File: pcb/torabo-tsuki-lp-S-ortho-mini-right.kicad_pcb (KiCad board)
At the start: 2 copper layers, 138.8 x 74 mm, 67 parts, among them J201 Conn_01x06_MountingPin, SW201 SW_SPDT, SW43 SW_Push, SW44 SW_Push, SW45 SW_Push, SW46 SW_Push, SW47 SW_Push, SW48 SW_Push, SW50 SW_Push, SW51 SW_Push, SW52 SW_Push, SW53 SW_Push, SW54 SW_Push, SW55 SW_Push, SW57 SW_Push, SW58 SW_Push, SW59 SW_Push, SW60 SW_Push, SW61 SW_Push, SW62 SW_Push, SW63 SW_Push, SW64 SW_Push, SW65 SW_Push, SW69 SW_Push, SW70 SW_Push, U201 XIAO nRF52840 Plus, U202 AE-XCL103-5V0, U203 XC8111AA01MR-G

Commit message: Rename PCB silkscreen to kb-1
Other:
- board text added: "kb-1"
- board text removed: "torabo-tsuki om(s) v0"
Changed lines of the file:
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@@
 		)
 	)
-	(gr_text "torabo-tsuki om(s) v0"
+	(gr_text "kb-1"
 		(at 43.1 150.9 0)
 		(layer "F.SilkS")

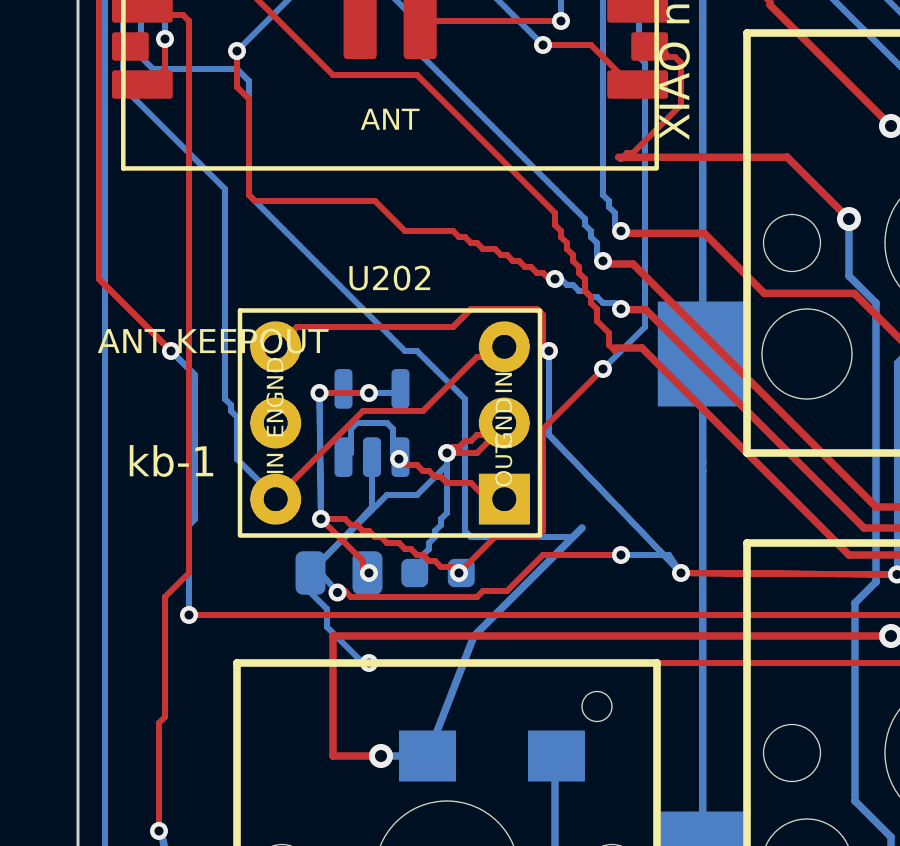
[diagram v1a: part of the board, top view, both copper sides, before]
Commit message: Add right-side boost circuit to PCBA
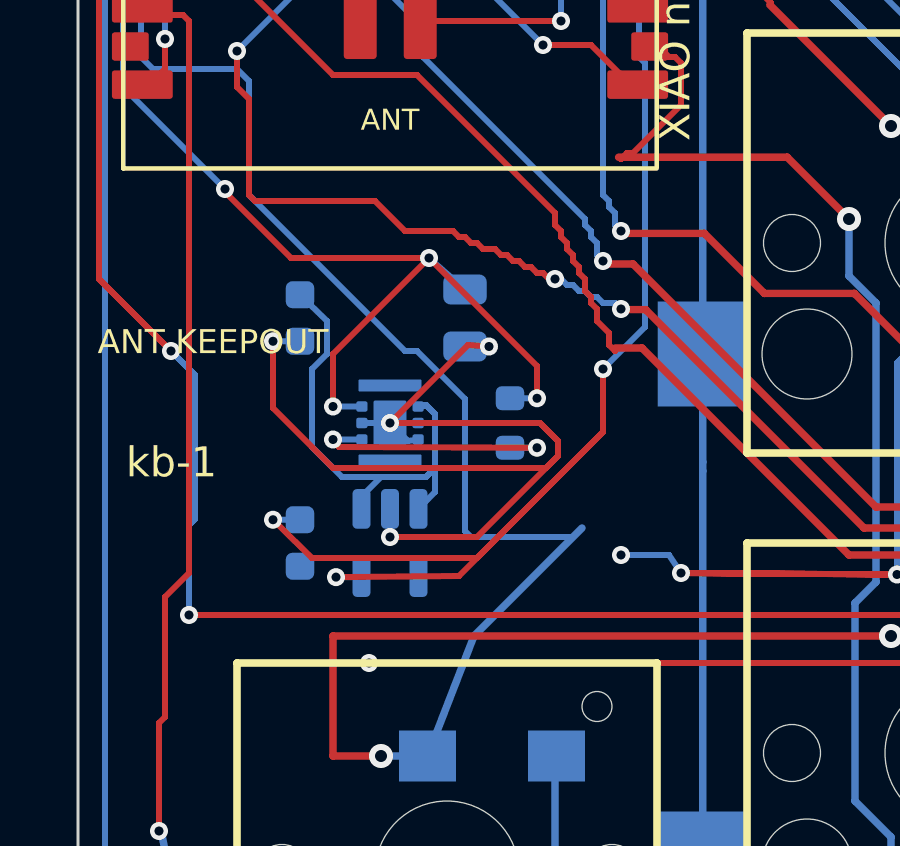
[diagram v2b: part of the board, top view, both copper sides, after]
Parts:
- added C204: 0.1uF 50V X7R, C_0603_1608Metric, B.Cu at (48.9, 153.0)
- added R202: 100k, R_0603_1608Metric, B.Cu at (55.9, 149.0)
- C202: value 0.1uF 50V X7R -> 10uF 16V X5R
- U202: value AE-XCL103-5V0 -> XCL103D503CR-G; footprint Library:AE-XCL103-5V0 -> CL-2025-02; moved to B.Cu
- moved C202 9.66 mm to (48.9, 145.5), turned to -90 degrees
- moved C201 9.48 mm to (54.4, 145.5), turned to -90 degrees
- moved U203 4.04 mm to (51.9, 153.0), turned to -90 degrees
- turned U202 to -90 degrees
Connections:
- C201 pad 1: /right/SYS_5V -> +BATT
- C202 pad 1: /right/SYS_5V -> /right/BOOST_5V
- U202 pad 1: GND -> +BATT
- U202 pad 2: (no net) -> GND
- U202 pad 3: +BATT -> /right/BOOST_EN
- U202 pad 4: +BATT -> GND
- U202 pad 5: GND -> (no net)
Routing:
- net GND: track 393.3 -> 358.5 mm, vias 17 -> 18
- net /right/BOOST_5V: track 8.26 -> 22.6 mm, vias 1 -> 0
- net /right/BOOST_EN: track 0.00 -> 8.78 mm, vias 0 -> 2
- net +BATT: track 50.5 -> 52.9 mm, vias 2 -> 6
- net /right/SYS_5V: track 57.5 -> 56.0 mm, vias 7 -> 4

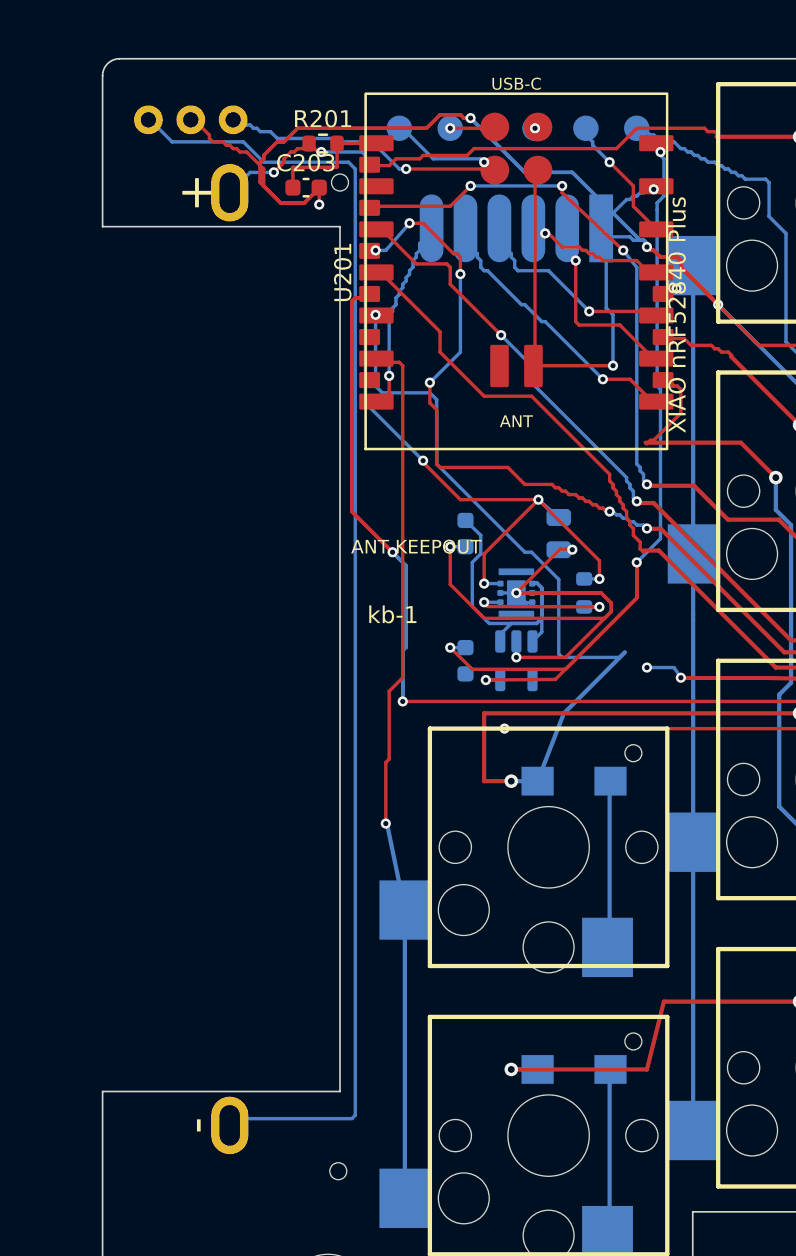
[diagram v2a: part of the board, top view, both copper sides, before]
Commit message: WIP: checkpoint single-XIAO PCB and vertical PHD conversion
Preserve the current single-controller PCB, schematics, documentation, and manufacturing artifacts. Include the vertical PHD placement/routing experiment; its candidate boards still fail DRC and are not production-ready.
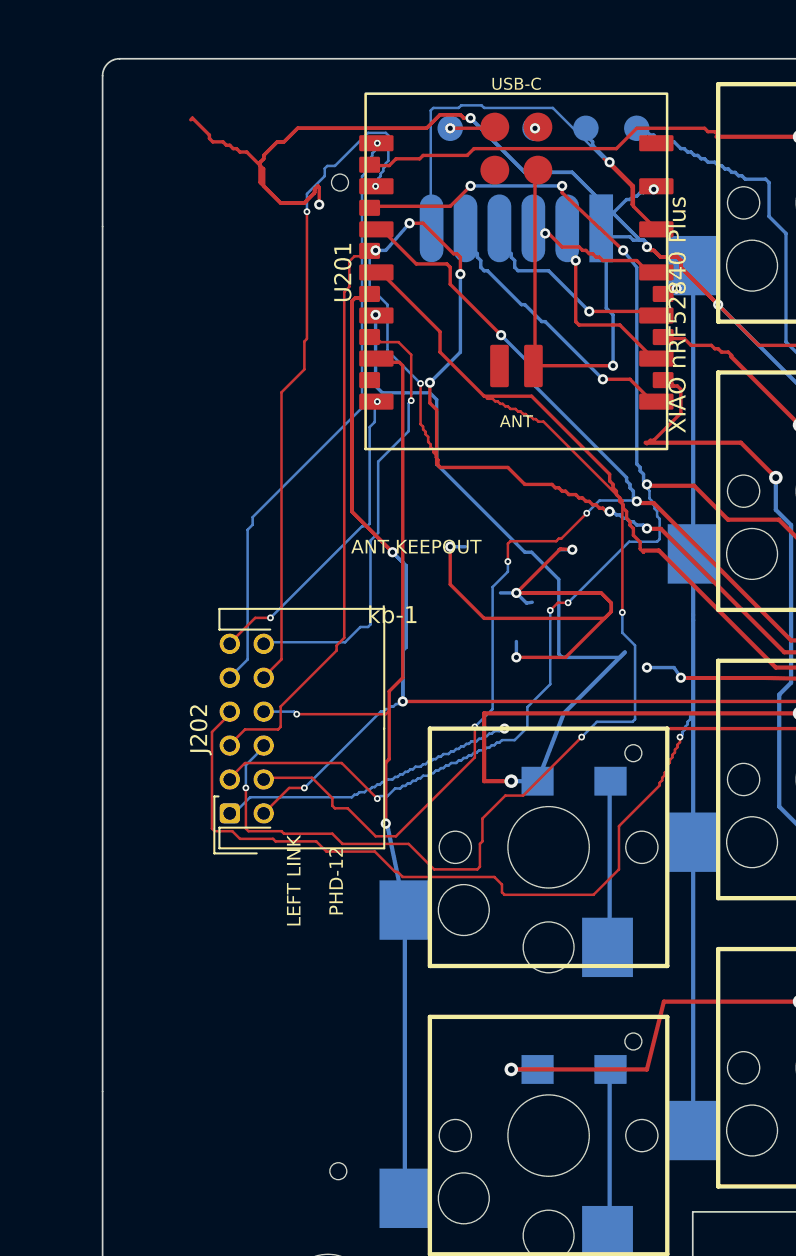
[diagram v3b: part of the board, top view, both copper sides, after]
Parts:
- removed BT201: GB-BH-4X1-WP, Library:battery_holder_AAA_1x_P55mm
- removed C201: 10uF 25V X5R, C_0805_2012Metric
- removed C202: 10uF 16V X5R, C_0603_1608Metric
- removed C203, C204: 0.1uF 50V X7R, C_0603_1608Metric
- removed R201: 10k, R_0603_1608Metric
- removed R202: 100k, R_0603_1608Metric
- removed SW201: SW_SPDT, Library:ISH-1260-HA-G
- removed TP203: RESET, TestPoint_Pad_D1.5mm
- removed U202: XCL103D503CR-G, CL-2025-02
- removed U203: XC8111AA01MR-G, SOT-23-5
- added J202: S12B-PHDSS, Connector_JST:JST_PHD_S12B-PHDSS_2x06_P2.00mm_Horizontal, F.Cu at (35.0, 162.0)
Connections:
- net /right/ROW1 renamed /right/RROW0
- net /right/ROW2 renamed /right/RROW1
- net /right/ROW3 renamed /right/RROW2
- net /right/ROW4 renamed /right/RROW3
- J201 pad 6: VCC -> /right/SYS_3V3
- U201 pad 1: /right/VBAT_ADC -> /right/LROW0
- U201 pad 14: /right/SYS_5V -> (no net)
- U201 pad 19: (no net) -> /right/LROW3
- U201 pad 2: /right/ROW0 -> /right/LROW1
- U201 pad 26: /right/RESET_N -> (no net)
- U201 pad 7: VCC -> /right/LROW2
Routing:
- net Net-(BT201--): track 77.0 -> 0.00 mm
- net /right/COL4: track 81.9 -> 140.3 mm, vias 1 -> 4
- net /right/SYS_5V: track 56.0 -> 0.00 mm, vias 4 -> 0
- net +BATT: track 52.9 -> 0.00 mm, vias 6 -> 0
- net /right/COL3: track 108.0 -> 156.2 mm, vias 7 -> 8
- net /right/COL5: track 53.8 -> 98.8 mm, vias 1 -> 2
- net /right/COL1: track 159.5 -> 199.3 mm, vias 5 -> 8
- net /right/LROW1: track 0.00 -> 39.6 mm, vias 0 -> 2
- net /right/COL2: track 115.9 -> 154.3 mm, vias 3 -> 6
- net /right/LROW0: track 0.00 -> 35.2 mm, vias 0 -> 1
- net /right/LROW3: track 0.00 -> 26.6 mm, vias 0 -> 1
- net /right/SYS_3V3: track 7.80 -> 32.0 mm
- net /right/RESET_N: track 23.5 -> 0.00 mm, vias 2 -> 0
- net /right/BOOST_5V: track 22.6 -> 0.00 mm
- net /right/LROW2: track 0.00 -> 18.6 mm, vias 0 -> 2
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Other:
- outline, holes or cut-outs redrawn
- board text added: "LEFT LINK"
- board text added: "PHD-12"

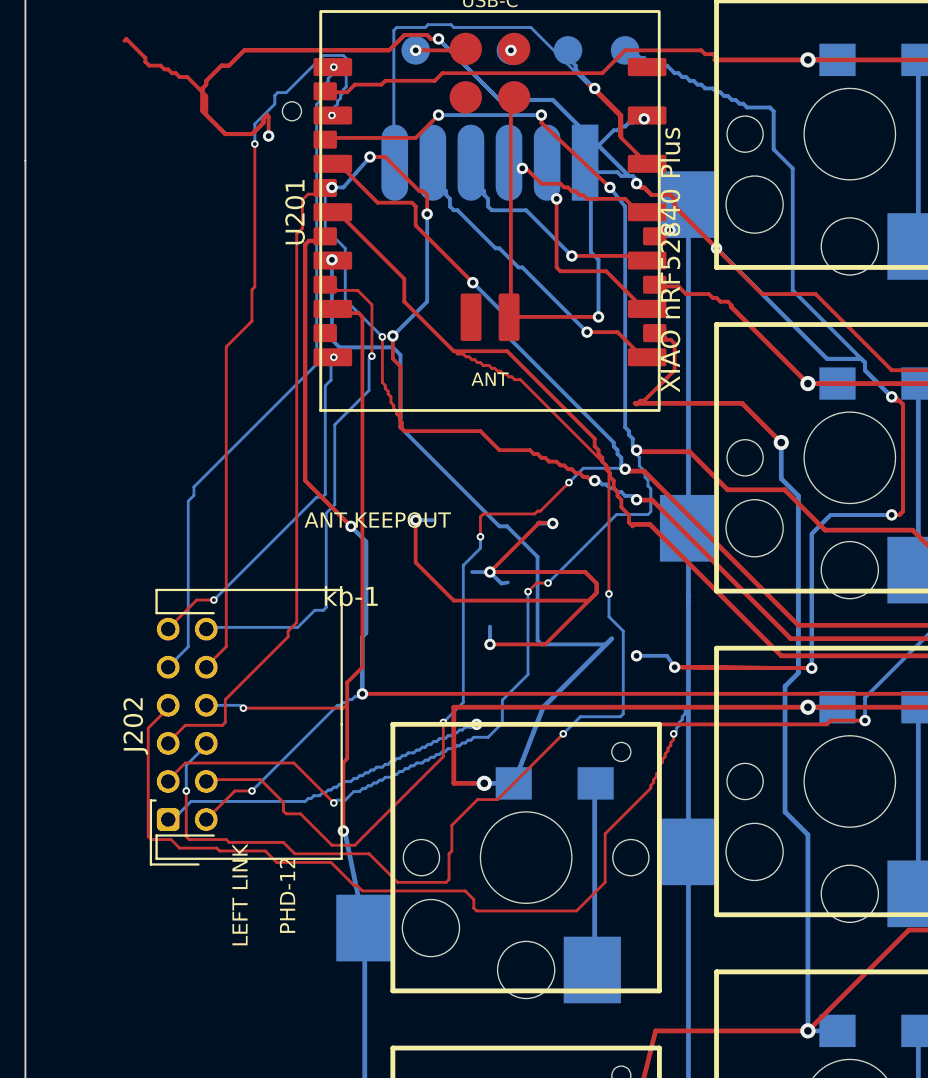
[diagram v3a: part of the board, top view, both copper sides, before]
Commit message: Use vertical JST PHD connectors on split PCBs
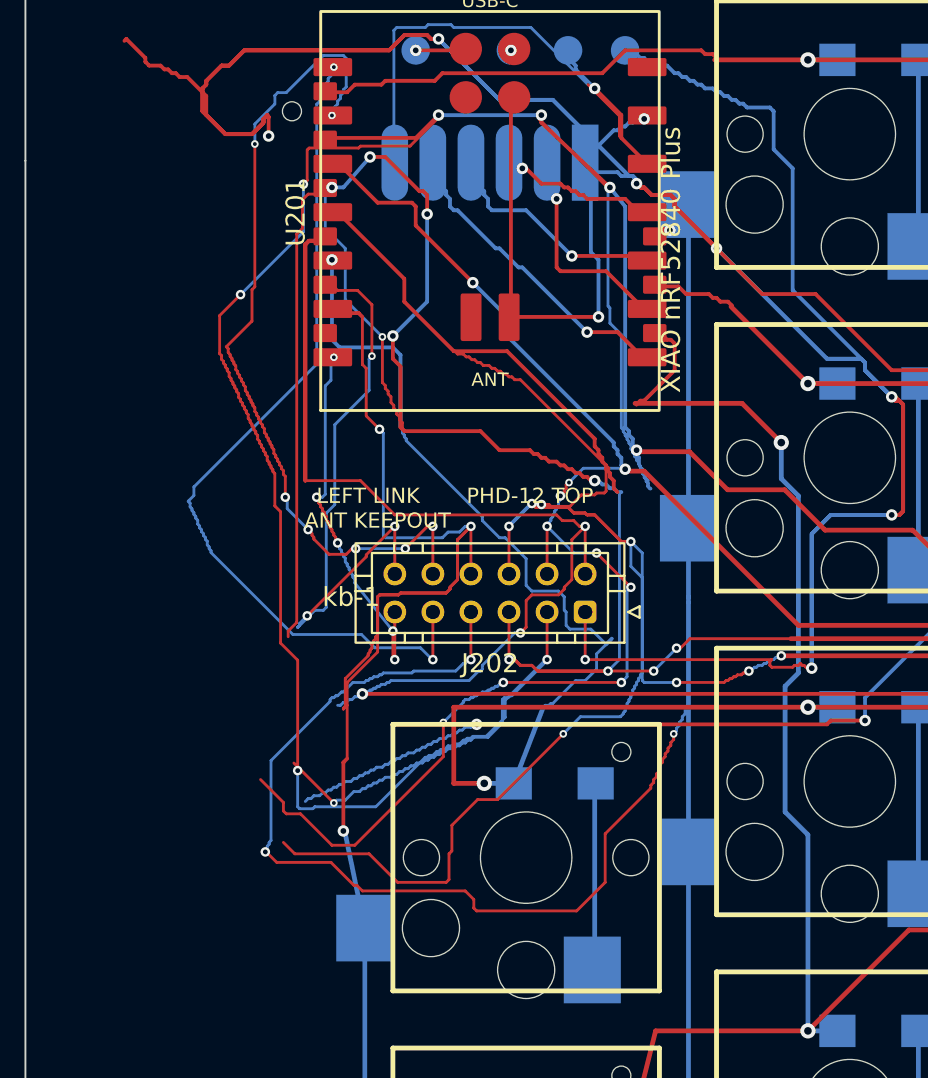
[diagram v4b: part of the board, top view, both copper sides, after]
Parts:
- J202: value S12B-PHDSS -> B12B-PHDSS; footprint Connector_JST:JST_PHD_S12B-PHDSS_2x06_P2.00mm_Horizontal -> Connector_JST:JST_PHD_B12B-PHDSS_2x06_P2.00mm_Vertical
- moved J202 24.5 mm to (56.9, 151.1), turned to 180 degrees
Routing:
- net /right/COL1: track 199.3 -> 272.5 mm, vias 8 -> 10
- net GND: track 376.7 -> 319.0 mm, vias 18 -> 13
- net /right/COL6: track 59.0 -> 78.9 mm, vias 2 -> 3
- net /right/COL4: track 140.3 -> 154.1 mm, vias 4 -> 9
- net /right/COL3: track 156.2 -> 168.0 mm, vias 8 -> 11
- net /right/LROW0: track 35.2 -> 45.7 mm, vias 1 -> 2
- net /right/COL2: track 154.3 -> 160.8 mm, vias 6 -> 11
- net /right/COL5: track 98.8 -> 105.2 mm, vias 2 -> 4
- net /right/LROW3: track 26.6 -> 31.6 mm, vias 1 -> 3
- net /right/LROW1: track 39.6 -> 44.0 mm, vias 2 -> 7
- net /right/LROW2: track 18.6 -> 20.5 mm, vias 2 -> 5
- net /right/COL0: track 217.7 -> 218.9 mm
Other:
- board text added: "PHD-12 TOP"
- board text removed: "PHD-12"

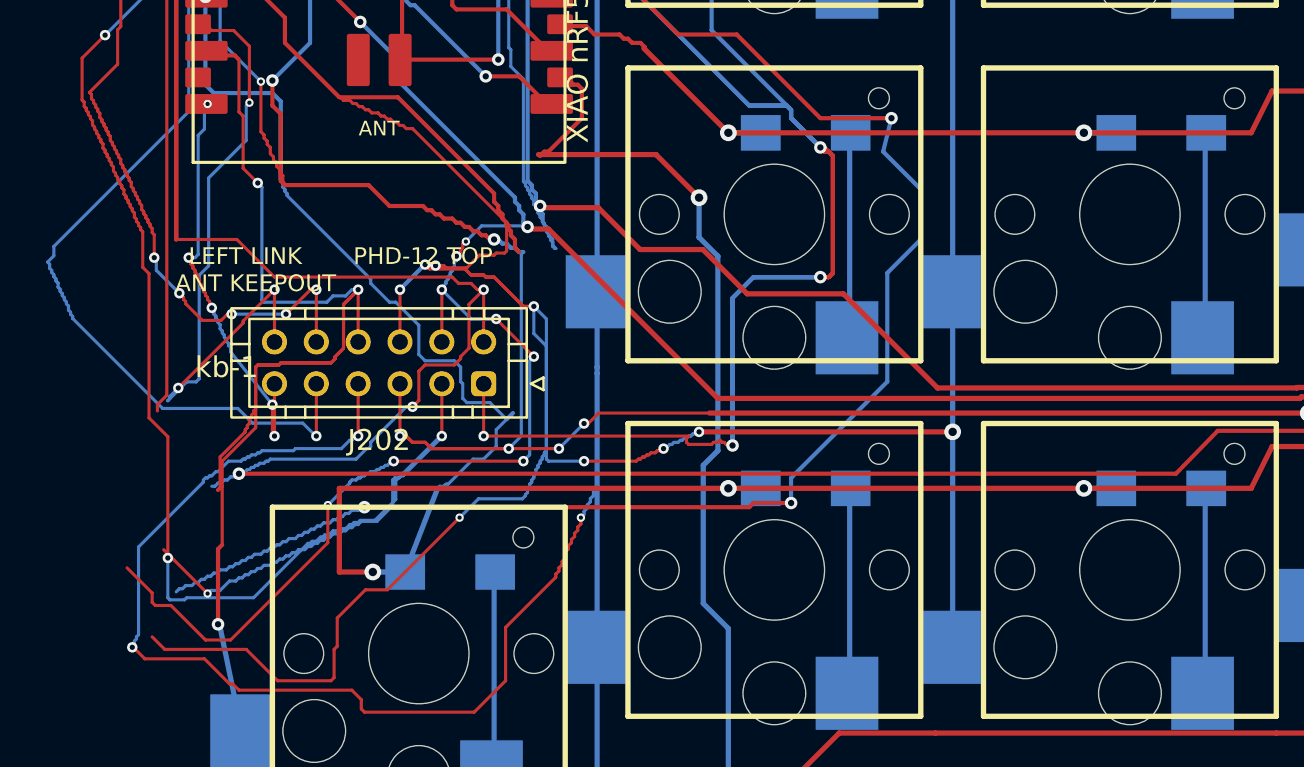
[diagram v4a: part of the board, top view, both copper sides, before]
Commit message: Replace split connectors with Samtec FFSD-compatible headers
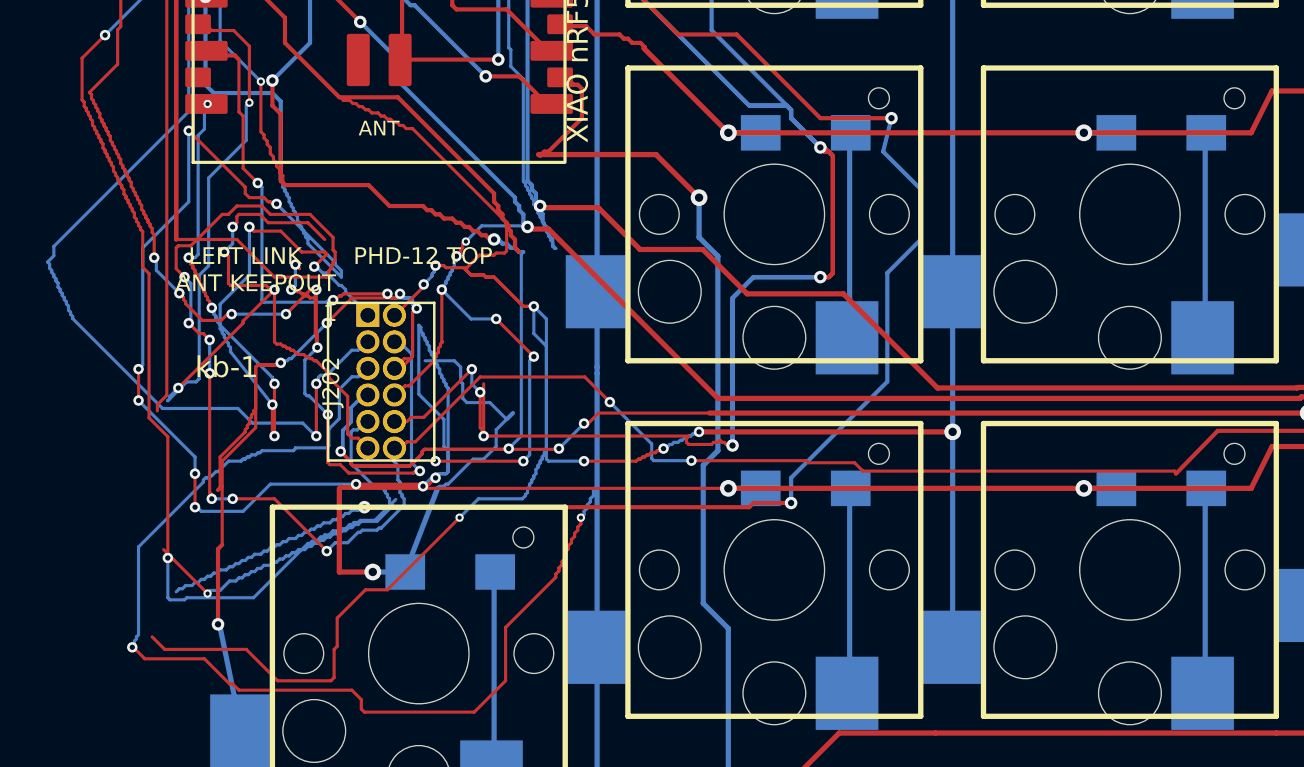
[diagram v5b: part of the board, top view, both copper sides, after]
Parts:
- J202: value B12B-PHDSS -> FTSH-106-01-L-D-K; footprint Connector_JST:JST_PHD_B12B-PHDSS_2x06_P2.00mm_Vertical -> Library:Samtec_FTSH-106-01-L-D-K
- moved J202 6.43 mm to (51.4, 147.8), turned to 0 degrees
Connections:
- J202 pad 1: GND -> /right/LROW2
- J202 pad 10: /right/LROW1 -> GND
- J202 pad 11: /right/LROW2 -> /right/LROW3
- J202 pad 12: /right/LROW3 -> /right/COL0
- J202 pad 2: /right/COL0 -> /right/COL4
- J202 pad 3: /right/COL1 -> /right/LROW0
- J202 pad 4: /right/COL2 -> /right/LROW1
- J202 pad 5: /right/COL3 -> /right/COL5
- J202 pad 6: /right/COL4 -> /right/COL6
- J202 pad 7: /right/COL5 -> /right/COL3
- J202 pad 8: /right/COL6 -> /right/COL2
- J202 pad 9: /right/LROW0 -> /right/COL1
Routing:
- net /right/RROW2: track 165.4 -> 224.0 mm, vias 8 -> 17
- net /right/LROW1: track 44.0 -> 67.6 mm, vias 7 -> 12
- net /right/LROW3: track 31.6 -> 50.1 mm, vias 3 -> 5
- net /right/LROW2: track 20.5 -> 38.4 mm, vias 5 -> 8
- net /right/COL2: track 160.8 -> 143.5 mm, vias 11 -> 10
- net /right/COL3: track 168.0 -> 178.9 mm
- net /right/COL4: track 154.1 -> 145.3 mm, vias 9 -> 8
- net GND: track 319.0 -> 327.2 mm, vias 13 -> 15
- net /right/COL1: track 272.5 -> 267.0 mm, vias 10 -> 9
- net /right/COL0: track 218.9 -> 223.8 mm, vias 4 -> 10
- net /right/LROW0: track 45.7 -> 49.2 mm, vias 2 -> 3
- net /right/COL6: track 78.9 -> 81.9 mm, vias 3 -> 8
- net /right/COL5: track 105.2 -> 105.9 mm, vias 4 -> 3
